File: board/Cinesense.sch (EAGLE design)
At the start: 7 parts, among them J1 AVR_SPI_PROG_3X2PTH, P1 DE9-PCB-EDGEMALE, P2 DE9-PCB-EDGEFEMALE, U1 ATTINY85-20PU

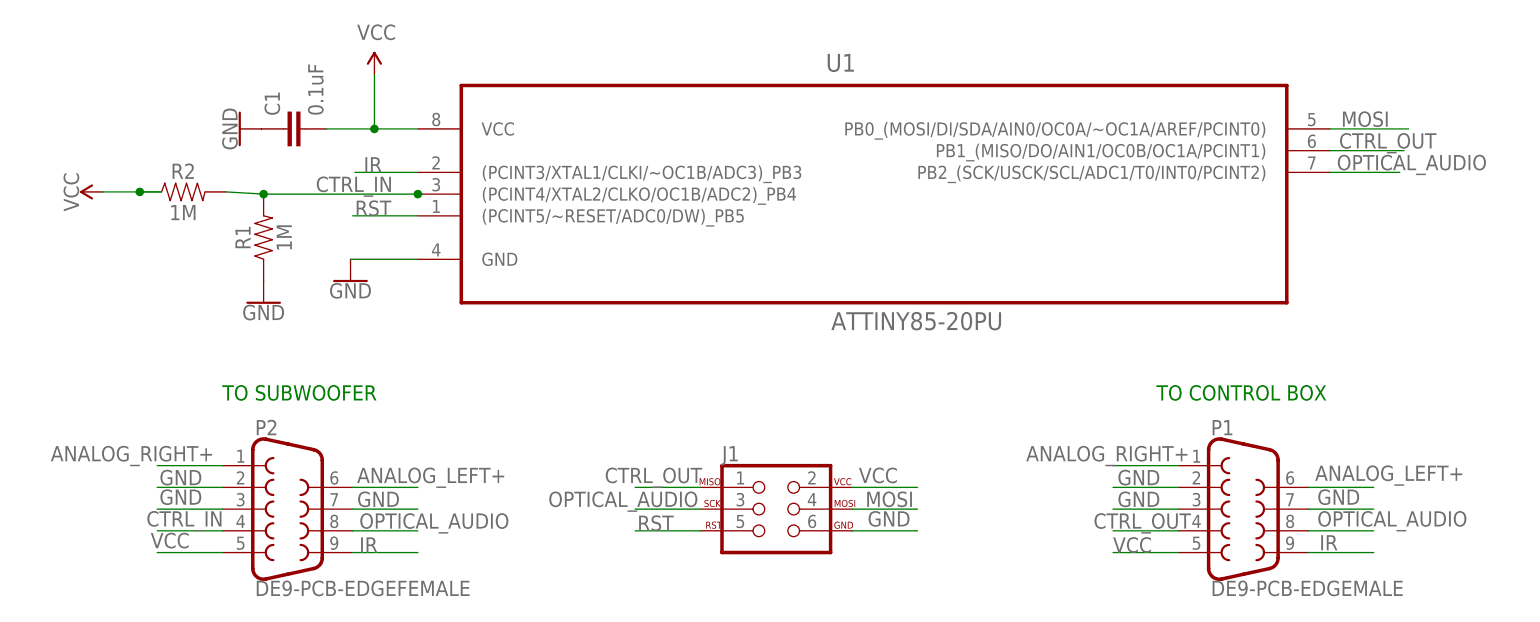
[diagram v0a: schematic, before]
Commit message: Connect analog audio signals to inputs
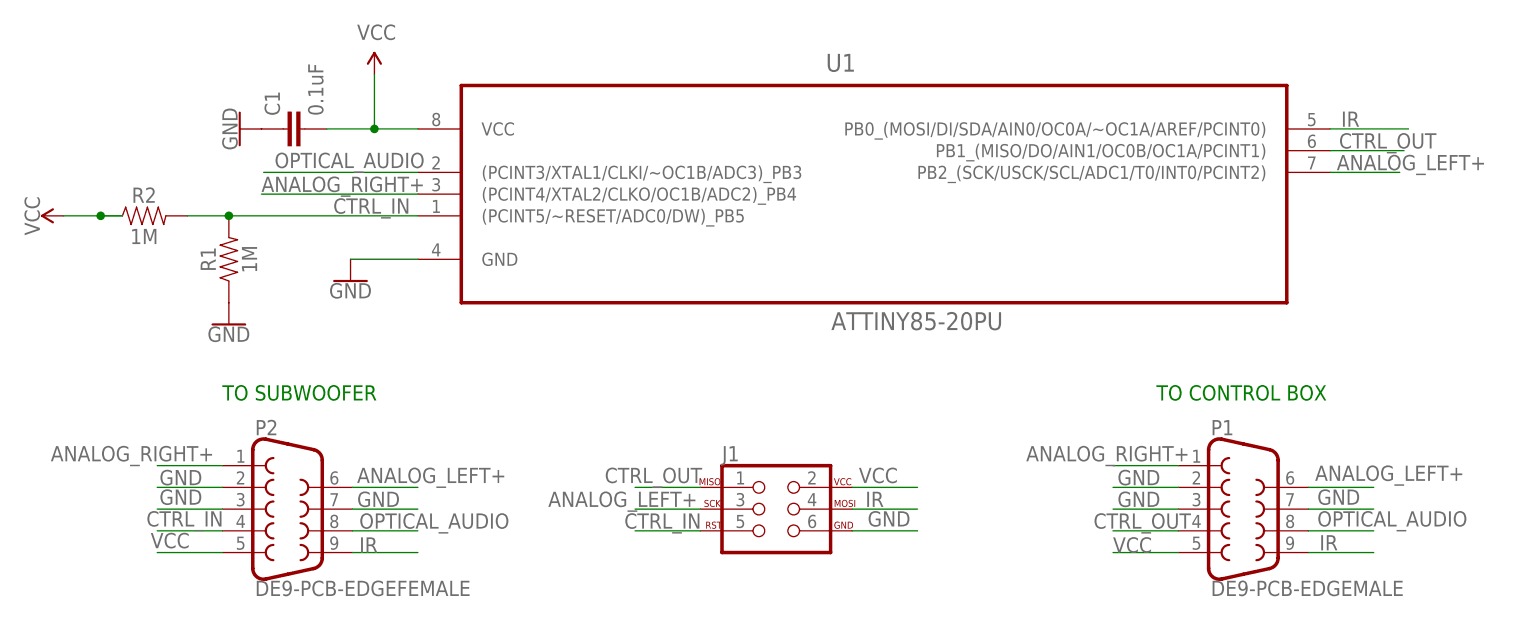
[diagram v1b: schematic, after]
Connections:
- removed net MOSI: J1.4, U1.PB0_(MOSI/DI/SDA/AIN0/OC0A/~OC1A/AREF/PCINT0)
- removed net RST: J1.5, U1.(PCINT5/~RESET/ADC0/DW)_PB5
- net ANALOG_LEFT+: now also J1.3, U1.PB2_(SCK/USCK/SCL/ADC1/T0/INT0/PCINT2)
- net ANALOG_RIGHT+: now also U1.(PCINT4/XTAL2/CLKO/OC1B/ADC2)_PB4
- net CTRL_IN: now also J1.5, U1.(PCINT5/~RESET/ADC0/DW)_PB5; no longer U1.(PCINT4/XTAL2/CLKO/OC1B/ADC2)_PB4
- net IR: now also J1.4, U1.PB0_(MOSI/DI/SDA/AIN0/OC0A/~OC1A/AREF/PCINT0); no longer U1.(PCINT3/XTAL1/CLKI/~OC1B/ADC3)_PB3
- net OPTICAL_AUDIO: now also U1.(PCINT3/XTAL1/CLKI/~OC1B/ADC3)_PB3; no longer J1.3, U1.PB2_(SCK/USCK/SCL/ADC1/T0/INT0/PCINT2)
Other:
- moved on the sheet: R1, R2
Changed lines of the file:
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@@
 <?xml version="1.0" encoding="utf-8"?>
 <!DOCTYPE eagle SYSTEM "eagle.dtd">
-<eagle version="9.3.1">
+<eagle version="9.6.2">
 <drawing>
 <settings>
@@
 <attribute name="NAME" x="-5.08" y="-9.652" size="1.778" layer="95" font="vector"/>
 </instance>
-<instance part="R1" gate="G$1" x="-58.674" y="16.51" smashed="yes" rot="R90">
-<attribute name="NAME" x="-60.198" y="16.51" size="1.778" layer="95" font="vector" rot="R90" align="bottom-center"/>
-<attribute name="VALUE" x="-57.15" y="16.51" size="1.778" layer="96" font="vector" rot="R90" align="top-center"/>
-</instance>
-<instance part="R2" gate="G$1" x="-68.072" y="21.844" smashed="yes">
-<attribute name="NAME" x="-68.072" y="23.368" size="1.778" layer="95" font="vector" align="bottom-center"/>
-<attribute name="VALUE" x="-68.072" y="20.32" size="1.778" layer="96" font="vector" align="top-center"/>
-</instance>
-<instance part="GND2" gate="1" x="-58.674" y="8.89" smashed="yes">
-<attribute name="VALUE" x="-58.674" y="8.636" size="1.778" layer="96" align="top-center"/>
-</instance>
-<instance part="SUPPLY1" gate="G$1" x="-77.47" y="21.844" smashed="yes" rot="R90">
-<attribute name="VALUE" x="-80.264" y="21.844" size="1.778" layer="96" rot="R90" align="bottom-center"/>
+<instance part="R1" gate="G$1" x="-62.738" y="13.97" smashed="yes" rot="R90">
+<attribute name="NAME" x="-64.262" y="13.97" size="1.778" layer="95" font="vector" rot="R90" align="bottom-center"/>
+<attribute name="VALUE" x="-61.214" y="13.97" size="1.778" layer="96" font="vector" rot="R90" align="top-center"/>
+</instance>
+<instance part="R2" gate="G$1" x="-72.644" y="19.05" smashed="yes">
+<attribute name="NAME" x="-72.644" y="20.574" size="1.778" layer="95" font="vector" align="bottom-center"/>
+<attribute name="VALUE" x="-72.644" y="17.526" size="1.778" layer="96" font="vector" align="top-center"/>
+</instance>
+<instance part="GND2" gate="1" x="-62.738" y="6.35" smashed="yes">
+<attribute name="VALUE" x="-62.738" y="6.096" size="1.778" layer="96" align="top-center"/>
+</instance>
+<instance part="SUPPLY1" gate="G$1" x="-82.042" y="19.05" smashed="yes" rot="R90">
+<attribute name="VALUE" x="-84.836" y="19.05" size="1.778" layer="96" rot="R90" align="bottom-center"/>
 </instance>
 <instance part="C1" gate="G$1" x="-53.848" y="29.21" smashed="yes" rot="R90">
@@
 </segment>
 </net>
-<net name="MOSI" class="0">
-<segment>
-<pinref part="J1" gate="G$1" pin="4"/>
-<wire x1="10.16" y1="-15.24" x2="17.78" y2="-15.24" width="0.1524" layer="91"/>
-<label x="11.684" y="-14.986" size="1.778" layer="95"/>
-</segment>
-<segment>
-<pinref part="U1" gate="A" pin="PB0_(MOSI/DI/SDA/AIN0/OC0A/~OC1A/AREF/PCINT0)"/>
-<wire x1="66.04" y1="29.21" x2="75.184" y2="29.21" width="0.1524" layer="91"/>
-<label x="67.31" y="29.464" size="1.778" layer="95"/>
-</segment>
-</net>
 <net name="VCC" class="0">
 <segment>
@@
 <segment>
 <pinref part="R2" gate="G$1" pin="1"/>
-<wire x1="-73.152" y1="21.844" x2="-70.612" y2="21.844" width="0.1524" layer="91"/>
+<wire x1="-77.724" y1="19.05" x2="-75.184" y2="19.05" width="0.1524" layer="91"/>
 <pinref part="SUPPLY1" gate="G$1" pin="VCC"/>
-<wire x1="-73.152" y1="21.844" x2="-77.47" y2="21.844" width="0.1524" layer="91"/>
-<junction x="-73.152" y="21.844"/>
+<wire x1="-77.724" y1="19.05" x2="-82.042" y2="19.05" width="0.1524" layer="91"/>
+<junction x="-77.724" y="19.05"/>
 </segment>
 <segment>
@@
 <label x="30.48" y="-9.652" size="1.778" layer="95"/>
 </segment>
+<segment>
+<pinref part="U1" gate="A" pin="(PCINT4/XTAL2/CLKO/OC1B/ADC2)_PB4"/>
+<wire x1="-40.64" y1="21.59" x2="-58.928" y2="21.59" width="0.1524" layer="91"/>
+<label x="-58.928" y="21.844" size="1.778" layer="95"/>
+</segment>
 </net>
 <net name="CTRL_IN" class="0">
@@
 </segment>
 <segment>
-<wire x1="-40.132" y1="21.59" x2="-40.64" y2="21.59" width="0.1524" layer="91"/>
-<wire x1="-40.64" y1="21.59" x2="-58.674" y2="21.59" width="0.1524" layer="91"/>
-<wire x1="-58.674" y1="21.59" x2="-62.992" y2="21.844" width="0.1524" layer="91"/>
+<pinref part="U1" gate="A" pin="(PCINT5/~RESET/ADC0/DW)_PB5"/>
+<wire x1="-40.64" y1="19.05" x2="-62.738" y2="19.05" width="0.1524" layer="91"/>
+<label x="-50.546" y="19.304" size="1.778" layer="95"/>
+<wire x1="-62.738" y1="19.05" x2="-67.564" y2="19.05" width="0.1524" layer="91"/>
 <pinref part="R1" gate="G$1" pin="2"/>
-<junction x="-58.674" y="21.59"/>
-<pinref part="U1" gate="A" pin="(PCINT4/XTAL2/CLKO/OC1B/ADC2)_PB4"/>
-<junction x="-40.64" y="21.59"/>
 <pinref part="R2" gate="G$1" pin="2"/>
-<label x="-52.578" y="21.844" size="1.778" layer="95"/>
+<junction x="-62.738" y="19.05"/>
+</segment>
+<segment>
+<pinref part="J1" gate="G$1" pin="5"/>
+<wire x1="-7.62" y1="-17.78" x2="-15.24" y2="-17.78" width="0.1524" layer="91"/>
+<label x="-16.51" y="-17.526" size="1.778" layer="95"/>
 </segment>
 </net>
@@
 <label x="64.262" y="-11.938" size="1.778" layer="95"/>
 </segment>
+<segment>
+<pinref part="U1" gate="A" pin="PB2_(SCK/USCK/SCL/ADC1/T0/INT0/PCINT2)"/>
+<wire x1="66.04" y1="24.13" x2="74.168" y2="24.13" width="0.1524" layer="91"/>
+<label x="66.802" y="24.384" size="1.778" layer="95"/>
+</segment>
+<segment>
+<pinref part="J1" gate="G$1" pin="3"/>
+<wire x1="-7.62" y1="-15.24" x2="-15.24" y2="-15.24" width="0.1524" layer="91"/>
+<label x="-25.4" y="-14.986" size="1.778" layer="95"/>
+</segment>
 </net>
 <net name="OPTICAL_AUDIO" class="0">
@@
 </segment>
 <segment>
-<pinref part="U1" gate="A" pin="PB2_(SCK/USCK/SCL/ADC1/T0/INT0/PCINT2)"/>
-<wire x1="66.04" y1="24.13" x2="74.168" y2="24.13" width="0.1524" layer="91"/>
-<label x="66.802" y="24.384" size="1.778" layer="95"/>
-</segment>
-<segment>
-<pinref part="J1" gate="G$1" pin="3"/>
-<wire x1="-7.62" y1="-15.24" x2="-15.24" y2="-15.24" width="0.1524" layer="91"/>
-<label x="-25.4" y="-14.986" size="1.778" layer="95"/>
+<pinref part="U1" gate="A" pin="(PCINT3/XTAL1/CLKI/~OC1B/ADC3)_PB3"/>
+<wire x1="-40.64" y1="24.13" x2="-58.674" y2="24.13" width="0.1524" layer="91"/>
+<label x="-57.404" y="24.638" size="1.778" layer="95"/>
 </segment>
 </net>
@@
 </segment>
 <segment>
-<pinref part="U1" gate="A" pin="(PCINT3/XTAL1/CLKI/~OC1B/ADC3)_PB3"/>
-<wire x1="-40.64" y1="24.13" x2="-48.006" y2="24.13" width="0.1524" layer="91"/>
-<label x="-46.99" y="24.13" size="1.778" layer="95"/>
-</segment>
-</net>
-<net name="RST" class="0">
-<segment>
-<pinref part="U1" gate="A" pin="(PCINT5/~RESET/ADC0/DW)_PB5"/>
-<wire x1="-40.64" y1="19.05" x2="-48.26" y2="19.05" width="0.1524" layer="91"/>
-<label x="-48.006" y="19.05" size="1.778" layer="95"/>
-</segment>
-<segment>
-<pinref part="J1" gate="G$1" pin="5"/>
-<wire x1="-7.62" y1="-17.78" x2="-15.24" y2="-17.78" width="0.1524" layer="91"/>
-<label x="-14.986" y="-17.78" size="1.778" layer="95"/>
-</segment>
-</net>
+<pinref part="J1" gate="G$1" pin="4"/>
+<wire x1="10.16" y1="-15.24" x2="17.78" y2="-15.24" width="0.1524" layer="91"/>
+<label x="11.684" y="-14.986" size="1.778" layer="95"/>
+</segment>
+<segment>
+<pinref part="U1" gate="A" pin="PB0_(MOSI/DI/SDA/AIN0/OC0A/~OC1A/AREF/PCINT0)"/>
+<wire x1="66.04" y1="29.21" x2="75.184" y2="29.21" width="0.1524" layer="91"/>
+<label x="67.31" y="29.464" size="1.778" layer="95"/>
+</segment>
+</net>
